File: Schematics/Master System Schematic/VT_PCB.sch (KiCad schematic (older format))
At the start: 34 parts, among them K13 Voltage Tap Relay, K14 Voltage Tap Relay, K15 Voltage Tap Relay, K16 Voltage Tap Relay, K17 Voltage Tap Relay, K18 Voltage Tap Relay, K19 Voltage Tap Relay, K20 Voltage Tap Relay, K21 Voltage Tap Relay, K22 Voltage Tap Relay

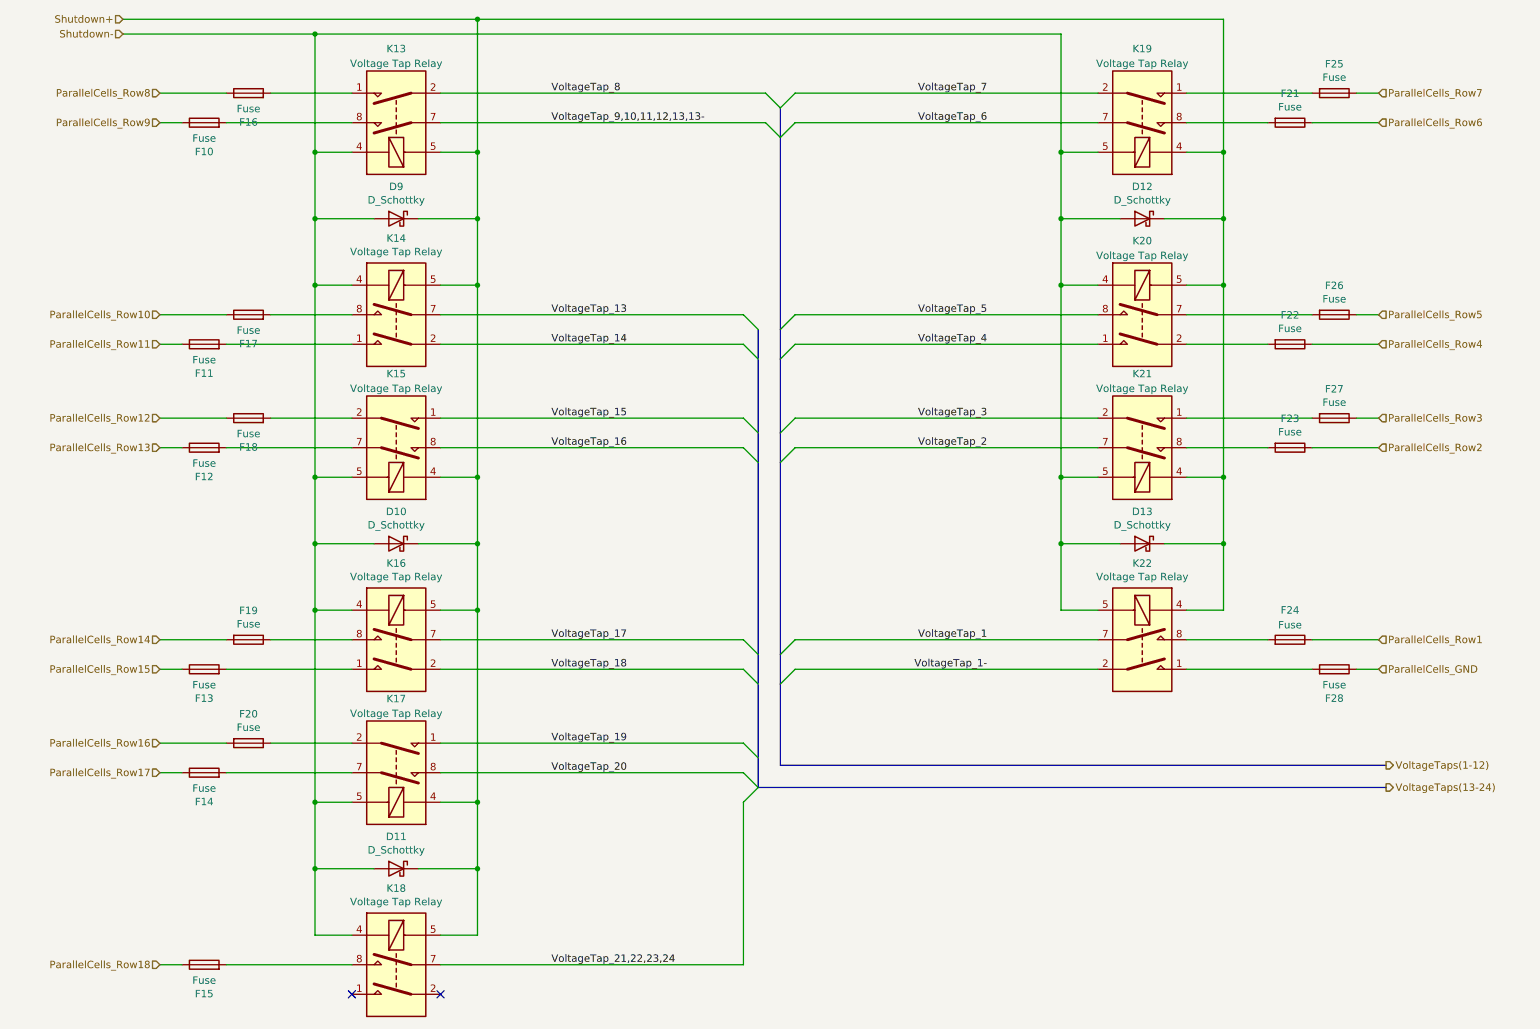
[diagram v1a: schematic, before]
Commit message: Added SD card module to brake light schematic
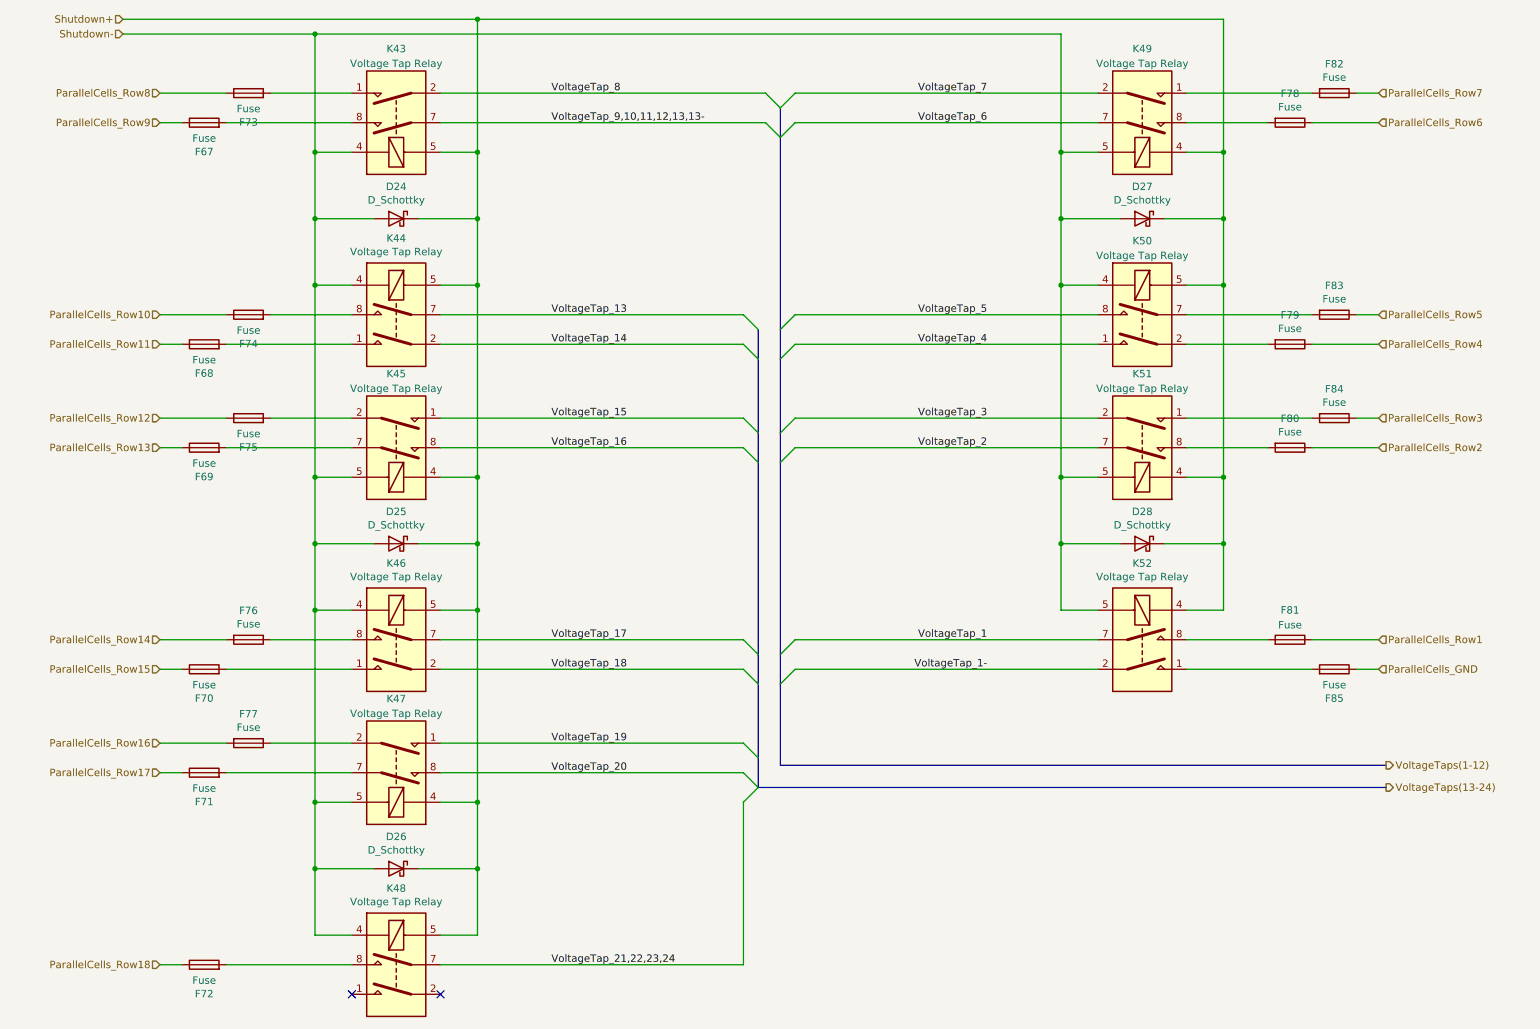
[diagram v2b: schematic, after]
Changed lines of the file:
@@
 AR Path="/5F45B05E/605AC384/6054A887" Ref="K35"  Part="1"
 AR Path="/5F45B05E/605B3BFB/6054A887" Ref="K45"  Part="1"
-F 0 "K15" H 2950 3250 50  0000 C CNN
+F 0 "K45" H 2950 3250 50  0000 C CNN
 F 1 "Voltage Tap Relay" H 2950 3350 50  0000 C CNN
 F 2 "Relay_THT:Relay_DPST_Fujitsu_FTR-F1A" H 2950 3350 50  0001 C CNN
@@
 AR Path="/5F45B05E/605AC384/6054A88D" Ref="K36"  Part="1"
 AR Path="/5F45B05E/605B3BFB/6054A88D" Ref="K46"  Part="1"
-F 0 "K16" H 2950 5567 50  0000 C CNN
+F 0 "K46" H 2950 5567 50  0000 C CNN
 F 1 "Voltage Tap Relay" H 2950 5476 50  0000 C CNN
 F 2 "Relay_THT:Relay_DPST_Fujitsu_FTR-F1A" H 2950 4650 50  0001 C CNN
@@
 AR Path="/5F45B05E/605AC384/6054A893" Ref="K37"  Part="1"
 AR Path="/5F45B05E/605B3BFB/6054A893" Ref="K47"  Part="1"
-F 0 "K17" H 2950 5450 50  0000 C CNN
+F 0 "K47" H 2950 5450 50  0000 C CNN
 F 1 "Voltage Tap Relay" H 2950 5550 50  0000 C CNN
 F 2 "Relay_THT:Relay_DPST_Fujitsu_FTR-F1A" H 2950 5550 50  0001 C CNN
@@
 AR Path="/5F45B05E/605AC384/6057794E" Ref="F51"  Part="1"
 AR Path="/5F45B05E/605B3BFB/6057794E" Ref="F70"  Part="1"
-F 0 "F13" V 1453 5250 50  0000 C CNN
+F 0 "F70" V 1453 5250 50  0000 C CNN
 F 1 "Fuse" V 1544 5250 50  0000 C CNN
 F 2 "" V 1580 5250 50  0001 C CNN
@@
 AR Path="/5F45B05E/605AC384/60579EA8" Ref="F50"  Part="1"
 AR Path="/5F45B05E/605B3BFB/60579EA8" Ref="F69"  Part="1"
-F 0 "F12" V 1453 3750 50  0000 C CNN
+F 0 "F69" V 1453 3750 50  0000 C CNN
 F 1 "Fuse" V 1544 3750 50  0000 C CNN
 F 2 "" V 1580 3750 50  0001 C CNN
@@
 AR Path="/5F45B05E/605AC384/60579EAE" Ref="F56"  Part="1"
 AR Path="/5F45B05E/605B3BFB/60579EAE" Ref="F75"  Part="1"
-F 0 "F18" V 1753 3550 50  0000 C CNN
+F 0 "F75" V 1753 3550 50  0000 C CNN
 F 1 "Fuse" V 1844 3550 50  0000 C CNN
 F 2 "" V 1880 3550 50  0001 C CNN
@@
 AR Path="/5F45B05E/605AC384/60579EB6" Ref="F49"  Part="1"
 AR Path="/5F45B05E/605B3BFB/60579EB6" Ref="F68"  Part="1"
-F 0 "F11" V 1453 3050 50  0000 C CNN
+F 0 "F68" V 1453 3050 50  0000 C CNN
 F 1 "Fuse" V 1544 3050 50  0000 C CNN
 F 2 "" V 1580 3050 50  0001 C CNN
@@
 AR Path="/5F45B05E/605AC384/60579EBC" Ref="F55"  Part="1"
 AR Path="/5F45B05E/605B3BFB/60579EBC" Ref="F74"  Part="1"
-F 0 "F17" V 1753 2850 50  0000 C CNN
+F 0 "F74" V 1753 2850 50  0000 C CNN
 F 1 "Fuse" V 1844 2850 50  0000 C CNN
 F 2 "" V 1880 2850 50  0001 C CNN
@@
 AR Path="/5F45B05E/605AC384/6057BB2B" Ref="F48"  Part="1"
 AR Path="/5F45B05E/605B3BFB/6057BB2B" Ref="F67"  Part="1"
-F 0 "F10" V 1453 1550 50  0000 C CNN
+F 0 "F67" V 1453 1550 50  0000 C CNN
 F 1 "Fuse" V 1544 1550 50  0000 C CNN
 F 2 "" V 1580 1550 50  0001 C CNN
@@
 AR Path="/5F45B05E/605AC384/6057BB31" Ref="F54"  Part="1"
 AR Path="/5F45B05E/605B3BFB/6057BB31" Ref="F73"  Part="1"
-F 0 "F16" V 1753 1350 50  0000 C CNN
+F 0 "F73" V 1753 1350 50  0000 C CNN
 F 1 "Fuse" V 1844 1350 50  0000 C CNN
 F 2 "" V 1880 1350 50  0001 C CNN
@@
 AR Path="/5F45B05E/605AC384/6057BB39" Ref="F63"  Part="1"
 AR Path="/5F45B05E/605B3BFB/6057BB39" Ref="F82"  Part="1"
-F 0 "F25" V 9103 1350 50  0000 C CNN
+F 0 "F82" V 9103 1350 50  0000 C CNN
 F 1 "Fuse" V 9194 1350 50  0000 C CNN
 F 2 "" V 9230 1350 50  0001 C CNN
@@
 AR Path="/5F45B05E/605AC384/6057BB3F" Ref="F59"  Part="1"
 AR Path="/5F45B05E/605B3BFB/6057BB3F" Ref="F78"  Part="1"
-F 0 "F21" V 8803 1550 50  0000 C CNN
+F 0 "F78" V 8803 1550 50  0000 C CNN
 F 1 "Fuse" V 8894 1550 50  0000 C CNN
 F 2 "" V 8930 1550 50  0001 C CNN
@@
 AR Path="/5F45B05E/605AC384/6057BB47" Ref="F64"  Part="1"
 AR Path="/5F45B05E/605B3BFB/6057BB47" Ref="F83"  Part="1"
-F 0 "F26" V 9103 2850 50  0000 C CNN
+F 0 "F83" V 9103 2850 50  0000 C CNN
 F 1 "Fuse" V 9194 2850 50  0000 C CNN
 F 2 "" V 9230 2850 50  0001 C CNN
@@
 AR Path="/5F45B05E/605AC384/6057BB4D" Ref="F60"  Part="1"
 AR Path="/5F45B05E/605B3BFB/6057BB4D" Ref="F79"  Part="1"
-F 0 "F22" V 8803 3050 50  0000 C CNN
+F 0 "F79" V 8803 3050 50  0000 C CNN
 F 1 "Fuse" V 8894 3050 50  0000 C CNN
 F 2 "" V 8930 3050 50  0001 C CNN
@@
 AR Path="/5F45B05E/605AC384/6057BB55" Ref="F65"  Part="1"
 AR Path="/5F45B05E/605B3BFB/6057BB55" Ref="F84"  Part="1"
-F 0 "F27" V 9103 3550 50  0000 C CNN
+F 0 "F84" V 9103 3550 50  0000 C CNN
 F 1 "Fuse" V 9194 3550 50  0000 C CNN
 F 2 "" V 9230 3550 50  0001 C CNN
@@
 AR Path="/5F45B05E/605AC384/6057BB5B" Ref="F61"  Part="1"
 AR Path="/5F45B05E/605B3BFB/6057BB5B" Ref="F80"  Part="1"
-F 0 "F23" V 8803 3750 50  0000 C CNN
+F 0 "F80" V 8803 3750 50  0000 C CNN
 F 1 "Fuse" V 8894 3750 50  0000 C CNN
 F 2 "" V 8930 3750 50  0001 C CNN
@@
 AR Path="/5F45B05E/605AC384/6057D363" Ref="F66"  Part="1"
 AR Path="/5F45B05E/605B3BFB/6057D363" Ref="F85"  Part="1"
-F 0 "F28" V 9103 5250 50  0000 C CNN
+F 0 "F85" V 9103 5250 50  0000 C CNN
 F 1 "Fuse" V 9194 5250 50  0000 C CNN
 F 2 "" V 9230 5250 50  0001 C CNN
@@
 AR Path="/5F45B05E/605AC384/6057D369" Ref="F62"  Part="1"
 AR Path="/5F45B05E/605B3BFB/6057D369" Ref="F81"  Part="1"
-F 0 "F24" V 9200 5050 50  0000 C CNN
+F 0 "F81" V 9200 5050 50  0000 C CNN
 F 1 "Fuse" V 9100 5050 50  0000 C CNN
 F 2 "" V 8930 5050 50  0001 C CNN
@@
 AR Path="/5F45B05E/605AC384/5FB6A078" Ref="D19"  Part="1"
 AR Path="/5F45B05E/605B3BFB/5FB6A078" Ref="D24"  Part="1"
-F 0 "D9" H 2950 2417 50  0000 C CNN
+F 0 "D24" H 2950 2417 50  0000 C CNN
 F 1 "D_Schottky" H 2950 2326 50  0000 C CNN
 F 2 "" H 2950 2200 50  0001 C CNN
@@
 AR Path="/5F45B05E/605AC384/5FB74EA7" Ref="D20"  Part="1"
 AR Path="/5F45B05E/605B3BFB/5FB74EA7" Ref="D25"  Part="1"
-F 0 "D10" H 2950 4617 50  0000 C CNN
+F 0 "D25" H 2950 4617 50  0000 C CNN
 F 1 "D_Schottky" H 2950 4526 50  0000 C CNN
 F 2 "" H 2950 4400 50  0001 C CNN
@@
 AR Path="/5F45B05E/605AC384/5FB78242" Ref="D23"  Part="1"
 AR Path="/5F45B05E/605B3BFB/5FB78242" Ref="D28"  Part="1"
-F 0 "D13" H 8000 4617 50  0000 C CNN
+F 0 "D28" H 8000 4617 50  0000 C CNN
 F 1 "D_Schottky" H 8000 4526 50  0000 C CNN
 F 2 "" H 8000 4400 50  0001 C CNN
@@
 AR Path="/5F45B05E/605AC384/5FB7A02F" Ref="D22"  Part="1"
 AR Path="/5F45B05E/605B3BFB/5FB7A02F" Ref="D27"  Part="1"
-F 0 "D12" H 8000 2417 50  0000 C CNN
+F 0 "D27" H 8000 2417 50  0000 C CNN
 F 1 "D_Schottky" H 8000 2326 50  0000 C CNN
 F 2 "" H 8000 2200 50  0001 C CNN
@@
 AR Path="/5F45B05E/605AC384/5FBDF245" Ref="K33"  Part="1"
 AR Path="/5F45B05E/605B3BFB/5FBDF245" Ref="K43"  Part="1"
-F 0 "K13" H 2950 1050 50  0000 C CNN
+F 0 "K43" H 2950 1050 50  0000 C CNN
 F 1 "Voltage Tap Relay" H 2950 1150 50  0000 C CNN
 F 2 "Relay_THT:Relay_DPST_Fujitsu_FTR-F1A" H 2950 1150 50  0001 C CNN
@@
 AR Path="/5F45B05E/605AC384/5FBDF24B" Ref="K39"  Part="1"
 AR Path="/5F45B05E/605B3BFB/5FBDF24B" Ref="K49"  Part="1"
-F 0 "K19" H 8000 1050 50  0000 C CNN
+F 0 "K49" H 8000 1050 50  0000 C CNN
 F 1 "Voltage Tap Relay" H 8000 1150 50  0000 C CNN
 F 2 "Relay_THT:Relay_DPST_Fujitsu_FTR-F1A" H 8000 1150 50  0001 C CNN
@@
 AR Path="/5F45B05E/605AC384/5FBDF251" Ref="K40"  Part="1"
 AR Path="/5F45B05E/605B3BFB/5FBDF251" Ref="K50"  Part="1"
-F 0 "K20" H 8000 3350 50  0000 C CNN
+F 0 "K50" H 8000 3350 50  0000 C CNN
 F 1 "Voltage Tap Relay" H 8000 3250 50  0000 C CNN
 F 2 "Relay_THT:Relay_DPST_Fujitsu_FTR-F1A" H 8000 2450 50  0001 C CNN
@@
 AR Path="/5F45B05E/605AC384/5FBDF257" Ref="K42"  Part="1"
 AR Path="/5F45B05E/605B3BFB/5FBDF257" Ref="K52"  Part="1"
-F 0 "K22" H 8000 5567 50  0000 C CNN
+F 0 "K52" H 8000 5567 50  0000 C CNN
 F 1 "Voltage Tap Relay" H 8000 5476 50  0000 C CNN
 F 2 "Relay_THT:Relay_DPST_Fujitsu_FTR-F1A" H 8000 4650 50  0001 C CNN
@@
 AR Path="/5F45B05E/605AC384/5FBDF25D" Ref="K41"  Part="1"
 AR Path="/5F45B05E/605B3BFB/5FBDF25D" Ref="K51"  Part="1"
-F 0 "K21" H 8000 3250 50  0000 C CNN
+F 0 "K51" H 8000 3250 50  0000 C CNN
 F 1 "Voltage Tap Relay" H 8000 3350 50  0000 C CNN
 F 2 "Relay_THT:Relay_DPST_Fujitsu_FTR-F1A" H 8000 3350 50  0001 C CNN
@@
 AR Path="/5F45B05E/605AC384/60548E5D" Ref="K34"  Part="1"
 AR Path="/5F45B05E/605B3BFB/60548E5D" Ref="K44"  Part="1"
-F 0 "K14" H 2950 3367 50  0000 C CNN
+F 0 "K44" H 2950 3367 50  0000 C CNN
 F 1 "Voltage Tap Relay" H 2950 3276 50  0000 C CNN
 F 2 "Relay_THT:Relay_DPST_Fujitsu_FTR-F1A" H 2950 2450 50  0001 C CNN
@@
 AR Path="/5F45B05E/605AC384/5FB76776" Ref="D21"  Part="1"
 AR Path="/5F45B05E/605B3BFB/5FB76776" Ref="D26"  Part="1"
-F 0 "D11" H 2950 6817 50  0000 C CNN
+F 0 "D26" H 2950 6817 50  0000 C CNN
 F 1 "D_Schottky" H 2950 6726 50  0000 C CNN
 F 2 "" H 2950 6600 50  0001 C CNN
@@
 AR Path="/5F45B05E/605AC384/5FC1EEB9" Ref="F53"  Part="1"
 AR Path="/5F45B05E/605B3BFB/5FC1EEB9" Ref="F72"  Part="1"
-F 0 "F15" V 1453 7250 50  0000 C CNN
+F 0 "F72" V 1453 7250 50  0000 C CNN
 F 1 "Fuse" V 1544 7250 50  0000 C CNN
 F 2 "" V 1580 7250 50  0001 C CNN
@@
 AR Path="/5F45B05E/605AC384/6054A899" Ref="K38"  Part="1"
 AR Path="/5F45B05E/605B3BFB/6054A899" Ref="K48"  Part="1"
-F 0 "K18" H 2950 7767 50  0000 C CNN
+F 0 "K48" H 2950 7767 50  0000 C CNN
 F 1 "Voltage Tap Relay" H 2950 7676 50  0000 C CNN
 F 2 "Relay_THT:Relay_DPST_Fujitsu_FTR-F1A" H 2950 6850 50  0001 C CNN
@@
 AR Path="/5F45B05E/605AC384/5FD0ECB2" Ref="F58"  Part="1"
 AR Path="/5F45B05E/605B3BFB/5FD0ECB2" Ref="F77"  Part="1"
-F 0 "F20" V 1753 5750 50  0000 C CNN
+F 0 "F77" V 1753 5750 50  0000 C CNN
 F 1 "Fuse" V 1844 5750 50  0000 C CNN
 F 2 "" V 1880 5750 50  0001 C CNN
@@
 AR Path="/5F45B05E/605AC384/5FD12DBC" Ref="F57"  Part="1"
 AR Path="/5F45B05E/605B3BFB/5FD12DBC" Ref="F76"  Part="1"
-F 0 "F19" V 1753 5050 50  0000 C CNN
+F 0 "F76" V 1753 5050 50  0000 C CNN
 F 1 "Fuse" V 1844 5050 50  0000 C CNN
 F 2 "" V 1880 5050 50  0001 C CNN
@@
 AR Path="/5F45B05E/605AC384/5FD210E5" Ref="F52"  Part="1"
 AR Path="/5F45B05E/605B3BFB/5FD210E5" Ref="F71"  Part="1"
-F 0 "F14" V 1453 5950 50  0000 C CNN
+F 0 "F71" V 1453 5950 50  0000 C CNN
 F 1 "Fuse" V 1544 5950 50  0000 C CNN
 F 2 "" V 1580 5950 50  0001 C CNN
